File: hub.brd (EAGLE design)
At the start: 64.1 x 51.7 mm, 50 parts, among them IC1 SN65220DBV, IC2 SN65220DBV, IC3 SN65220DBV, IC4 SN65220DBV, IC5 SN65220DBV, U1 LM3526-L, X1 12MHz

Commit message: pick ferrite beads
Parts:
- LB2, LB3, LB4, LB5: value (none) -> 220
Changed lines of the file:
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@@
 <attribute name="VALUE" value="100uF" x="59.7" y="13.4" size="1.778" layer="27" rot="R90" display="off"/>
 </element>
-<element name="LB2" library="rcl" library_urn="urn:adsk.eagle:library:334" package="R0805" package3d_urn="urn:adsk.eagle:package:23553/2" value="" x="62.977" y="28.718" rot="R270"/>
+<element name="LB2" library="rcl" library_urn="urn:adsk.eagle:library:334" package="R0805" package3d_urn="urn:adsk.eagle:package:23553/2" value="220" x="62.977" y="28.718" rot="R270">
+<attribute name="DIGIKEY" value="490-1054-1-ND" x="62.977" y="28.718" size="1.778" layer="27" rot="R270" display="off"/>
+<attribute name="MPN" value="BLM21PG221SN1D" x="62.977" y="28.718" size="1.778" layer="27" rot="R270" display="off"/>
+<attribute name="OC_MOUSER" value="81-BLM21P221SG" x="62.977" y="28.718" size="1.778" layer="27" rot="R270" display="off"/>
+</element>
 <element name="C16" library="rcl" library_urn="urn:adsk.eagle:library:334" package="C0805" package3d_urn="urn:adsk.eagle:package:23617/2" value="0.1uF" x="47.608" y="14.741"/>
 <element name="EC2" library="rcl" library_urn="urn:adsk.eagle:library:334" package="UD-5X5,8_NICHICON" package3d_urn="urn:adsk.eagle:package:23470/1" value="4.3uF" x="42.4" y="19" rot="R270">
@@
 <attribute name="VALUE" value="100uF" x="59.5" y="22.2" size="1.778" layer="27" rot="R90" display="off"/>
 </element>
-<element name="LB3" library="rcl" library_urn="urn:adsk.eagle:library:334" package="R0805" package3d_urn="urn:adsk.eagle:package:23553/2" value="" x="58.565" y="26.512"/>
+<element name="LB3" library="rcl" library_urn="urn:adsk.eagle:library:334" package="R0805" package3d_urn="urn:adsk.eagle:package:23553/2" value="220" x="58.565" y="26.512">
+<attribute name="DIGIKEY" value="490-1054-1-ND" x="58.565" y="26.512" size="1.778" layer="27" display="off"/>
+<attribute name="MPN" value="BLM21PG221SN1D" x="58.565" y="26.512" size="1.778" layer="27" display="off"/>
+<attribute name="OC_MOUSER" value="81-BLM21P221SG" x="58.565" y="26.512" size="1.778" layer="27" display="off"/>
+</element>
 <element name="IC2" library="sn65220_40" package="SOT23-6" value="SN65220DBV" x="43.248" y="38.338" rot="R270"/>
 <element name="C1" library="rcl" library_urn="urn:adsk.eagle:library:334" package="C0805" package3d_urn="urn:adsk.eagle:package:23617/2" value="0.1uF" x="30.996" y="34.976" rot="MR0"/>
@@
 <attribute name="VALUE" value="100uF" x="27.1" y="11.4" size="1.778" layer="27" rot="R180" display="off"/>
 </element>
-<element name="LB4" library="rcl" library_urn="urn:adsk.eagle:library:334" package="R0805" package3d_urn="urn:adsk.eagle:package:23553/2" value="" x="22.5" y="8.53" rot="R90"/>
+<element name="LB4" library="rcl" library_urn="urn:adsk.eagle:library:334" package="R0805" package3d_urn="urn:adsk.eagle:package:23553/2" value="220" x="22.5" y="8.53" rot="R90">
+<attribute name="DIGIKEY" value="490-1054-1-ND" x="22.5" y="8.53" size="1.778" layer="27" rot="R90" display="off"/>
+<attribute name="MPN" value="BLM21PG221SN1D" x="22.5" y="8.53" size="1.778" layer="27" rot="R90" display="off"/>
+<attribute name="OC_MOUSER" value="81-BLM21P221SG" x="22.5" y="8.53" size="1.778" layer="27" rot="R90" display="off"/>
+</element>
 <element name="IC4" library="sn65220_40" package="SOT23-6" value="SN65220DBV" x="9.817" y="20.127" rot="R180"/>
 <element name="C22" library="rcl" library_urn="urn:adsk.eagle:library:334" package="C0805" package3d_urn="urn:adsk.eagle:package:23617/2" value="0.1uF" x="19.588" y="2.742" rot="R90"/>
@@
 <attribute name="VALUE" value="100uF" x="27" y="3.7" size="1.778" layer="27" rot="R180" display="off"/>
 </element>
-<element name="LB5" library="rcl" library_urn="urn:adsk.eagle:library:334" package="R0805" package3d_urn="urn:adsk.eagle:package:23553/2" value="" x="22.569" y="2.742" rot="R90"/>
+<element name="LB5" library="rcl" library_urn="urn:adsk.eagle:library:334" package="R0805" package3d_urn="urn:adsk.eagle:package:23553/2" value="220" x="22.569" y="2.742" rot="R90">
+<attribute name="DIGIKEY" value="490-1054-1-ND" x="22.569" y="2.742" size="1.778" layer="27" rot="R90" display="off"/>
+<attribute name="MPN" value="BLM21PG221SN1D" x="22.569" y="2.742" size="1.778" layer="27" rot="R90" display="off"/>
+<attribute name="OC_MOUSER" value="81-BLM21P221SG" x="22.569" y="2.742" size="1.778" layer="27" rot="R90" display="off"/>
+</element>
 <element name="IC5" library="sn65220_40" package="SOT23-6" value="SN65220DBV" x="21.174" y="13.664" rot="R180"/>
 <element name="C3" library="rcl" library_urn="urn:adsk.eagle:library:334" package="C0805" package3d_urn="urn:adsk.eagle:package:23617/2" value="1uF" x="37.2" y="27.3" rot="MR180"/>

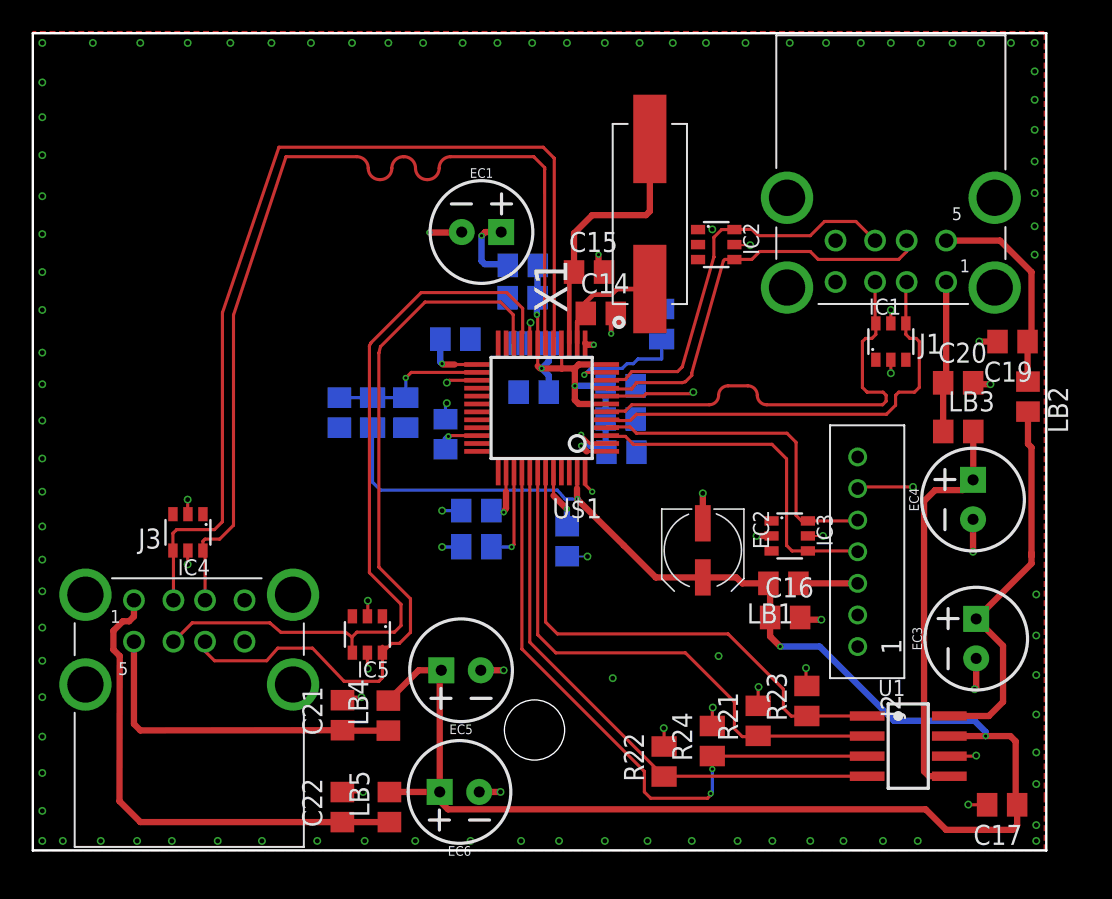
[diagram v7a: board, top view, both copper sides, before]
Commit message: pick USB transient suppressors
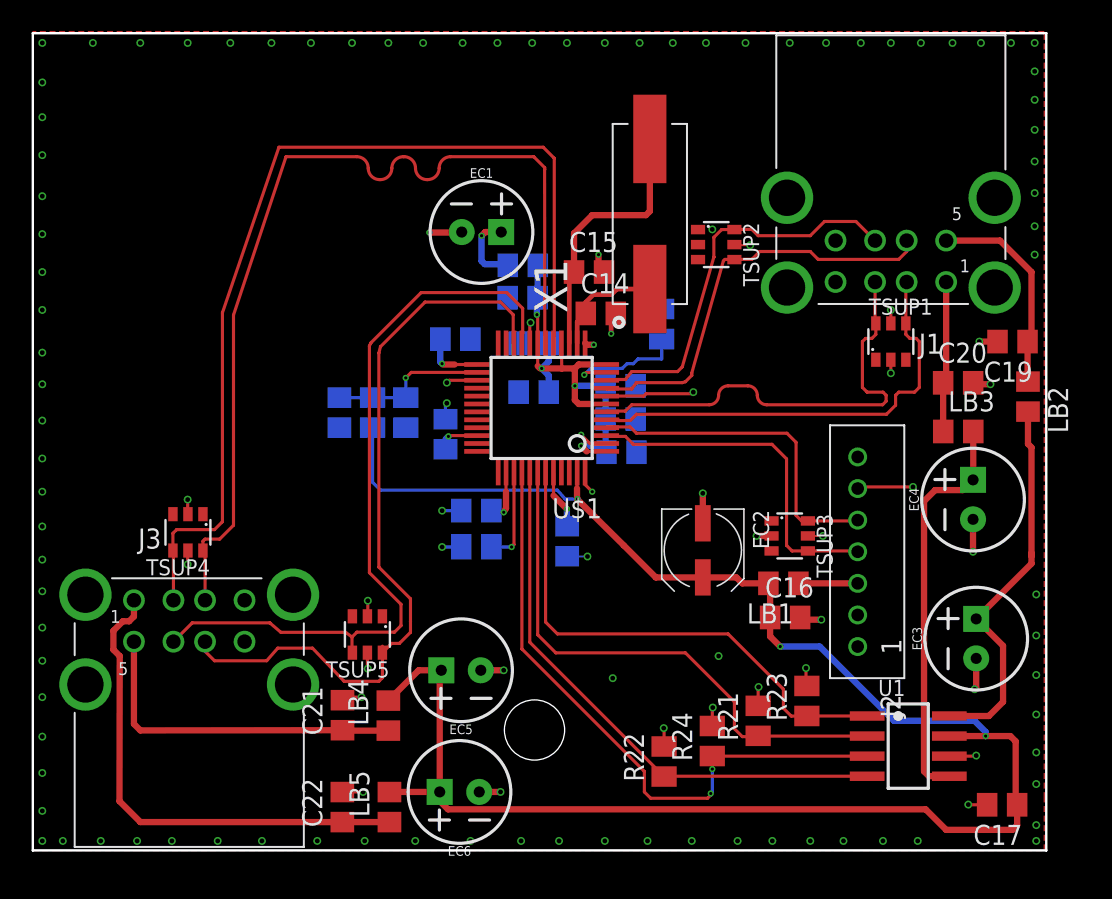
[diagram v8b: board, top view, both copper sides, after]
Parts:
- renumbered IC1 to TSUP1, IC2 to TSUP2, IC3 to TSUP3, IC4 to TSUP4, IC5 to TSUP5
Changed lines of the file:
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@@
 <attribute name="OC_MOUSER" value="647-UUP1C4R7MCL1GS" x="42.4" y="19" size="1.778" layer="27" rot="R270" display="off"/>
 </element>
-<element name="IC1" library="sn65220_40" package="SOT23-6" value="SN65220DBV" x="54.3" y="32.2"/>
+<element name="TSUP1" library="sn65220_40" package="SOT23-6" value="SN65220DBV" x="54.3" y="32.2">
+<attribute name="DIGIKEY" value="296-9694-1-ND" x="54.3" y="32.2" size="1.778" layer="27" display="off"/>
+<attribute name="MPN" value="SN65220DBVR" x="54.3" y="32.2" size="1.778" layer="27" display="off"/>
+<attribute name="OC_MOUSER" value="595-SN65220DBVR" x="54.3" y="32.2" size="1.778" layer="27" display="off"/>
+</element>
 <element name="C20" library="rcl" library_urn="urn:adsk.eagle:library:334" package="C0805" package3d_urn="urn:adsk.eagle:package:23617/2" value="0.1uF" x="58.559" y="29.59"/>
 <element name="EC4" library="SparkFun-Capacitors" library_urn="urn:adsk.eagle:library:510" package="CPOL-RADIAL-2.5MM-6.5MM" package3d_urn="urn:adsk.eagle:package:37415/1" value="120uF" x="59.5" y="22.2" rot="R90">
@@
 <attribute name="OC_MOUSER" value="81-BLM21P221SG" x="58.565" y="26.512" size="1.778" layer="27" display="off"/>
 </element>
-<element name="IC2" library="sn65220_40" package="SOT23-6" value="SN65220DBV" x="43.248" y="38.338" rot="R270"/>
+<element name="TSUP2" library="sn65220_40" package="SOT23-6" value="SN65220DBV" x="43.248" y="38.338" rot="R270">
+<attribute name="DIGIKEY" value="296-9694-1-ND" x="43.248" y="38.338" size="1.778" layer="27" rot="R270" display="off"/>
+<attribute name="MPN" value="SN65220DBVR" x="43.248" y="38.338" size="1.778" layer="27" rot="R270" display="off"/>
+<attribute name="OC_MOUSER" value="595-SN65220DBVR" x="43.248" y="38.338" size="1.778" layer="27" rot="R270" display="off"/>
+</element>
 <element name="C1" library="rcl" library_urn="urn:adsk.eagle:library:334" package="C0805" package3d_urn="urn:adsk.eagle:package:23617/2" value="0.1uF" x="30.996" y="34.976" rot="MR0"/>
 <element name="EC1" library="SparkFun-Capacitors" library_urn="urn:adsk.eagle:library:510" package="CPOL-RADIAL-2.5MM-6.5MM" package3d_urn="urn:adsk.eagle:package:37415/1" value="10uF" x="28.392" y="39.132">
@@
 <element name="R23" library="rcl" library_urn="urn:adsk.eagle:library:334" package="M0805" package3d_urn="urn:adsk.eagle:package:23556/1" value="100K" x="48.986" y="9.457" rot="R90"/>
 <element name="R24" library="rcl" library_urn="urn:adsk.eagle:library:334" package="M0805" package3d_urn="urn:adsk.eagle:package:23556/1" value="10K" x="43" y="6.922" rot="R90"/>
-<element name="IC3" library="sn65220_40" package="SOT23-6" value="SN65220DBV" x="47.9" y="19.9" rot="R270"/>
+<element name="TSUP3" library="sn65220_40" package="SOT23-6" value="SN65220DBV" x="47.9" y="19.9" rot="R270">
+<attribute name="DIGIKEY" value="296-9694-1-ND" x="47.9" y="19.9" size="1.778" layer="27" rot="R270" display="off"/>
+<attribute name="MPN" value="SN65220DBVR" x="47.9" y="19.9" size="1.778" layer="27" rot="R270" display="off"/>
+<attribute name="OC_MOUSER" value="595-SN65220DBVR" x="47.9" y="19.9" size="1.778" layer="27" rot="R270" display="off"/>
+</element>
 <element name="LB1" library="rcl" library_urn="urn:adsk.eagle:library:334" package="R0805" package3d_urn="urn:adsk.eagle:package:23553/2" value="" x="47.5" y="16.9" rot="R180"/>
 <element name="C12" library="rcl" library_urn="urn:adsk.eagle:library:334" package="C0805" package3d_urn="urn:adsk.eagle:package:23617/2" value="0.1uF" x="28.064" y="21.504" rot="MR0"/>
@@
 <attribute name="OC_MOUSER" value="81-BLM21P221SG" x="22.5" y="8.53" size="1.778" layer="27" rot="R90" display="off"/>
 </element>
-<element name="IC4" library="sn65220_40" package="SOT23-6" value="SN65220DBV" x="9.817" y="20.127" rot="R180"/>
+<element name="TSUP4" library="sn65220_40" package="SOT23-6" value="SN65220DBV" x="9.817" y="20.127" rot="R180">
+<attribute name="DIGIKEY" value="296-9694-1-ND" x="9.817" y="20.127" size="1.778" layer="27" rot="R180" display="off"/>
+<attribute name="MPN" value="SN65220DBVR" x="9.817" y="20.127" size="1.778" layer="27" rot="R180" display="off"/>
+<attribute name="OC_MOUSER" value="595-SN65220DBVR" x="9.817" y="20.127" size="1.778" layer="27" rot="R180" display="off"/>
+</element>
 <element name="C22" library="rcl" library_urn="urn:adsk.eagle:library:334" package="C0805" package3d_urn="urn:adsk.eagle:package:23617/2" value="0.1uF" x="19.588" y="2.742" rot="R90"/>
 <element name="EC6" library="SparkFun-Capacitors" library_urn="urn:adsk.eagle:library:510" package="CPOL-RADIAL-2.5MM-6.5MM" package3d_urn="urn:adsk.eagle:package:37415/1" value="120uF" x="27" y="3.7" rot="R180">
@@
 <attribute name="OC_MOUSER" value="81-BLM21P221SG" x="22.569" y="2.742" size="1.778" layer="27" rot="R90" display="off"/>
 </element>
-<element name="IC5" library="sn65220_40" package="SOT23-6" value="SN65220DBV" x="21.174" y="13.664" rot="R180"/>
+<element name="TSUP5" library="sn65220_40" package="SOT23-6" value="SN65220DBV" x="21.174" y="13.664" rot="R180">
+<attribute name="DIGIKEY" value="296-9694-1-ND" x="21.174" y="13.664" size="1.778" layer="27" rot="R180" display="off"/>
+<attribute name="MPN" value="SN65220DBVR" x="21.174" y="13.664" size="1.778" layer="27" rot="R180" display="off"/>
+<attribute name="OC_MOUSER" value="595-SN65220DBVR" x="21.174" y="13.664" size="1.778" layer="27" rot="R180" display="off"/>
+</element>
 <element name="C3" library="rcl" library_urn="urn:adsk.eagle:library:334" package="C0805" package3d_urn="urn:adsk.eagle:package:23617/2" value="1uF" x="37.2" y="27.3" rot="MR180"/>
 </elements>
@@
 <contactref element="EC2" pad="-"/>
 <contactref element="C16" pad="2"/>
-<contactref element="IC1" pad="5"/>
-<contactref element="IC1" pad="2"/>
+<contactref element="TSUP1" pad="5"/>
+<contactref element="TSUP1" pad="2"/>
 <contactref element="J1" pad="4"/>
 <contactref element="C20" pad="2"/>
 <contactref element="EC4" pad="2"/>
-<contactref element="IC2" pad="5"/>
-<contactref element="IC2" pad="2"/>
+<contactref element="TSUP2" pad="5"/>
+<contactref element="TSUP2" pad="2"/>
 <contactref element="EC1" pad="2"/>
 <contactref element="C1" pad="2"/>
@@
 <contactref element="C17" pad="2"/>
 <contactref element="U1" pad="6"/>
-<contactref element="IC3" pad="5"/>
-<contactref element="IC3" pad="2"/>
+<contactref element="TSUP3" pad="5"/>
+<contactref element="TSUP3" pad="2"/>
 <contactref element="C12" pad="2"/>
 <polygon width="0.125" layer="1" isolate="0.3048">
@@
 <contactref element="U$1" pad="37"/>
 <contactref element="U$1" pad="27"/>
-<contactref element="IC4" pad="5"/>
-<contactref element="IC4" pad="2"/>
-<contactref element="IC5" pad="5"/>
-<contactref element="IC5" pad="2"/>
+<contactref element="TSUP4" pad="5"/>
+<contactref element="TSUP4" pad="2"/>
+<contactref element="TSUP5" pad="5"/>
+<contactref element="TSUP5" pad="2"/>
 <contactref element="J3" pad="8"/>
 <contactref element="C21" pad="2"/>
@@
 <signal name="D0_N" class="1">
 <contactref element="U$1" pad="3"/>
-<contactref element="IC3" pad="4"/>
+<contactref element="TSUP3" pad="4"/>
 <contactref element="J2" pad="4"/>
 <wire x1="38" y1="25.7" x2="46.77573125" y2="25.7" width="0.2" layer="1"/>
@@
 <signal name="D0_P" class="1">
 <contactref element="U$1" pad="4"/>
-<contactref element="IC3" pad="6"/>
+<contactref element="TSUP3" pad="6"/>
 <contactref element="J2" pad="5"/>
 <wire x1="38.2" y1="26.4" x2="47.72426875" y2="26.4" width="0.2" layer="1"/>
@@
 <contactref element="U$1" pad="5"/>
 <contactref element="J1" pad="2"/>
-<contactref element="IC1" pad="4"/>
+<contactref element="TSUP1" pad="4"/>
 <wire x1="54.02426875" y1="27.6" x2="38.2" y2="27.6" width="0.2" layer="1"/>
 <wire x1="38.2" y1="27.6" x2="37.8" y2="27.2" width="0.2" layer="1"/>
@@
 <contactref element="U$1" pad="6"/>
 <contactref element="J1" pad="3"/>
-<contactref element="IC1" pad="6"/>
+<contactref element="TSUP1" pad="6"/>
 <wire x1="53.77573125" y1="28.2" x2="46.447440625" y2="28.2" width="0.2" layer="1"/>
 <wire x1="46.447440625" y1="28.2" x2="45.847440625" y2="28.8" width="0.2" layer="1" curve="-90"/>
@@
 <contactref element="U$1" pad="9"/>
 <contactref element="J1" pad="6"/>
-<contactref element="IC2" pad="4"/>
+<contactref element="TSUP2" pad="4"/>
 <wire x1="55.3" y1="38.59" x2="55.3" y2="37.9" width="0.2" layer="1"/>
 <wire x1="55.3" y1="37.9" x2="54.8" y2="37.4" width="0.2" layer="1"/>
@@
 <contactref element="U$1" pad="10"/>
 <contactref element="J1" pad="7"/>
-<contactref element="IC2" pad="6"/>
+<contactref element="TSUP2" pad="6"/>
 <wire x1="53.3" y1="38.59" x2="52.09" y2="39.8" width="0.2" layer="1"/>
 <wire x1="52.09" y1="39.8" x2="50.1" y2="39.8" width="0.2" layer="1"/>
@@
 <contactref element="U$1" pad="17"/>
 <contactref element="J3" pad="2"/>
-<contactref element="IC4" pad="4"/>
+<contactref element="TSUP4" pad="4"/>
 <wire x1="8.9" y1="15.83" x2="8.9" y2="18.944" width="0.2" layer="1"/>
 <wire x1="8.9" y1="18.944" x2="8.867" y2="18.977" width="0.2" layer="1"/>
@@
 <contactref element="U$1" pad="18"/>
 <contactref element="J3" pad="3"/>
-<contactref element="IC4" pad="6"/>
+<contactref element="TSUP4" pad="6"/>
 <wire x1="10.9" y1="15.83" x2="10.9" y2="18.844" width="0.2" layer="1"/>
 <wire x1="10.9" y1="18.844" x2="10.767" y2="18.977" width="0.2" layer="1"/>
@@
 <contactref element="U$1" pad="21"/>
 <contactref element="J3" pad="6"/>
-<contactref element="IC5" pad="4"/>
+<contactref element="TSUP5" pad="4"/>
 <wire x1="30" y1="35.3" x2="24.57573125" y2="35.3" width="0.2" layer="1"/>
 <wire x1="24.57573125" y1="35.3" x2="21.4" y2="32.12426875" width="0.2" layer="1"/>
@@
 <contactref element="U$1" pad="22"/>
 <contactref element="J3" pad="7"/>
-<contactref element="IC5" pad="6"/>
+<contactref element="TSUP5" pad="6"/>
 <wire x1="29.6" y1="34.7" x2="24.82426875" y2="34.7" width="0.2" layer="1"/>
 <wire x1="24.82426875" y1="34.7" x2="22" y2="31.87573125" width="0.2" layer="1"/>
